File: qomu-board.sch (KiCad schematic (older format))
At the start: 37 parts, among them IC1 EOS-S3, SW2 Captouch Pads, U1 LDO-X2SON-1.2V, U10 RGB-LED, U2 LDO-X2SON-3.3V, U3 LDO-X2SON-2.5V, U4 GD25Q16CEIGR, U5 MC3635, U9 USB-B

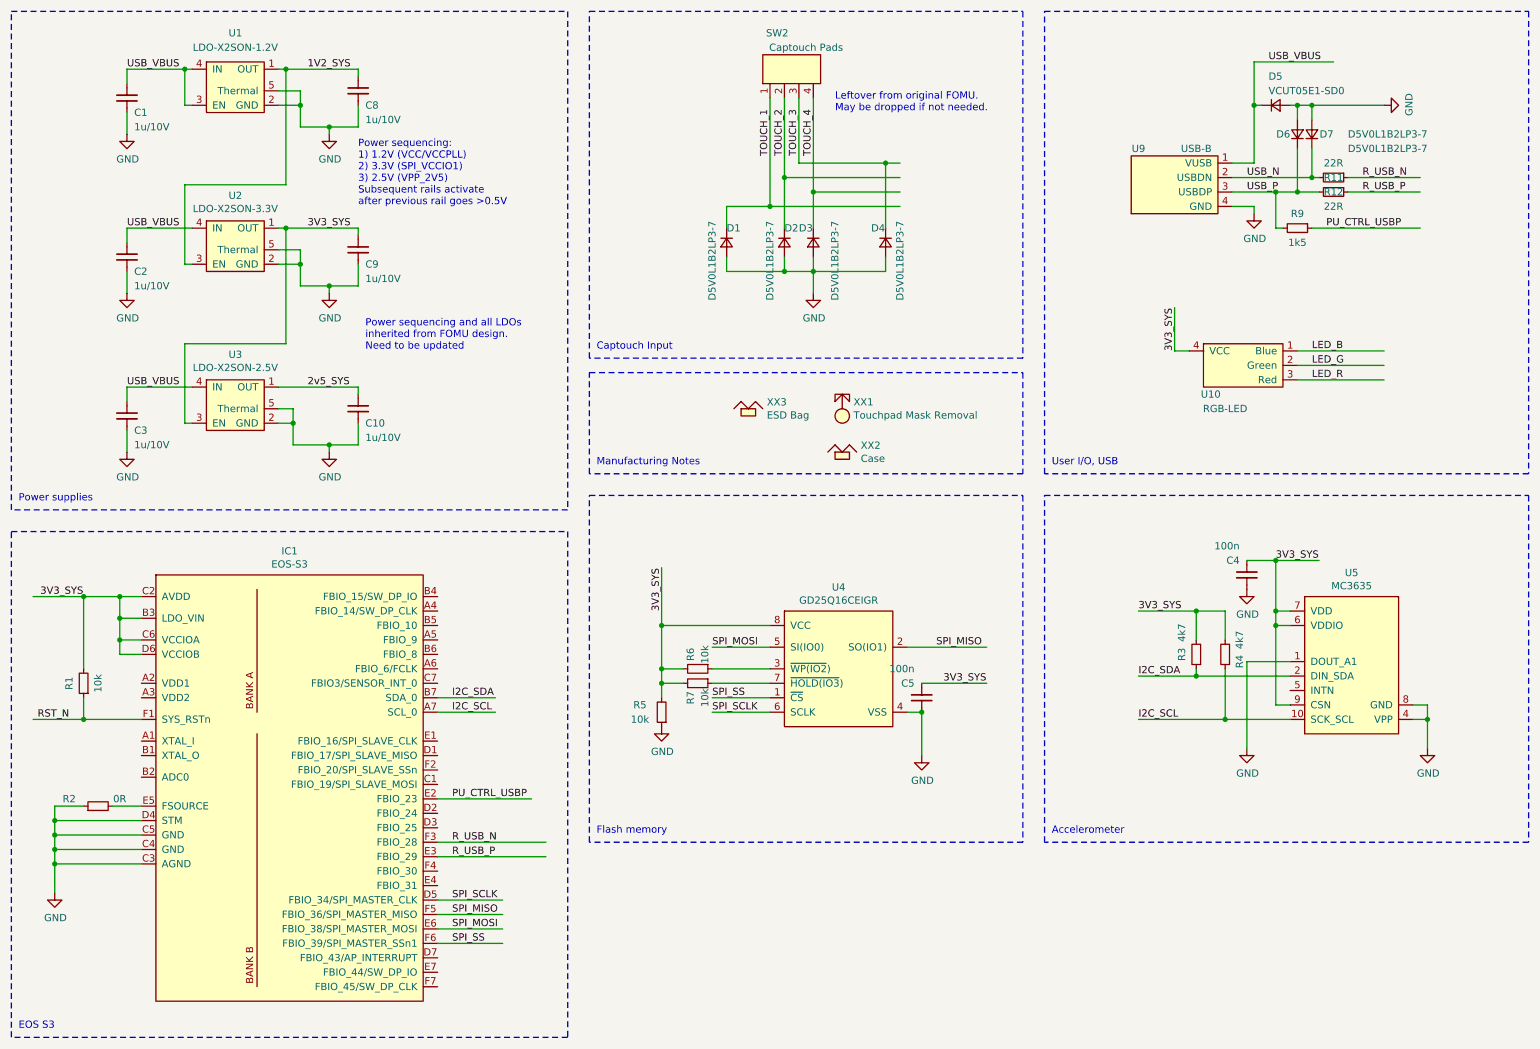
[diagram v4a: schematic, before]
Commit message: Added single LDO as power supply, cleanup
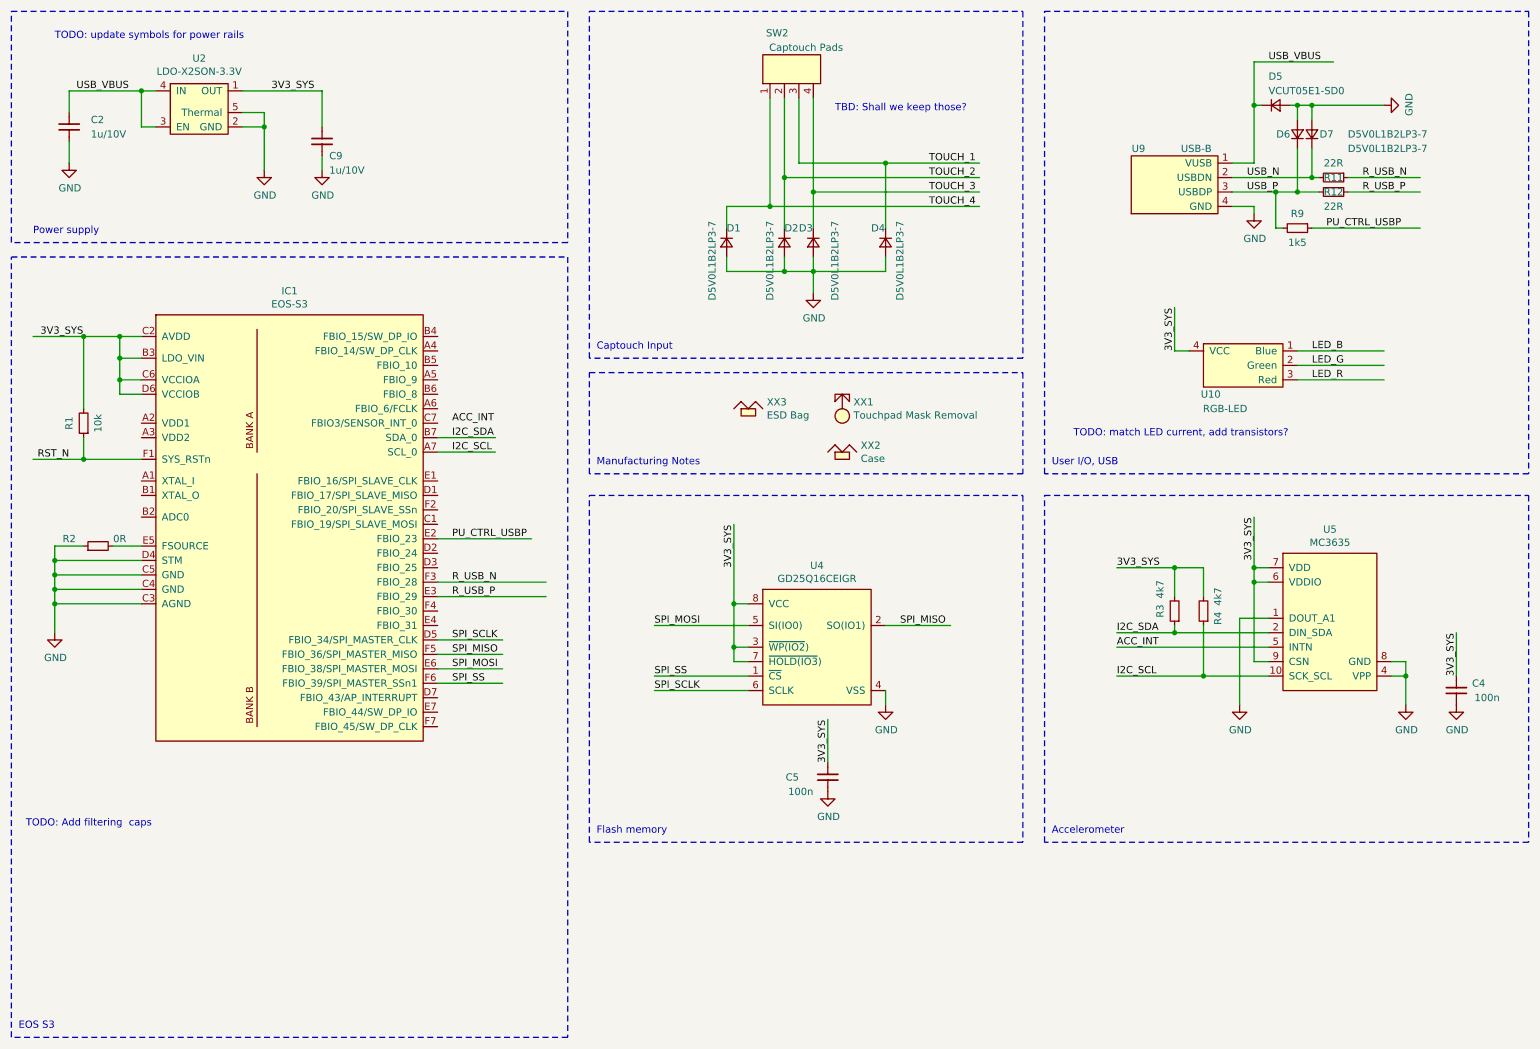
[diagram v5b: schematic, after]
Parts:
- removed C1, C10, C3, C8: 1u/10V, qomu-board:C_0201_0603Metric, symbol qomu-board:C_Small-Device
- removed R5, R6, R7: 10k, qomu-board:R_0201_0603Metric, symbol qomu-board:R_Small-Device
- removed U1: LDO-X2SON-1.2V, qomu-board:Texas_X2SON-4_1x1mm_P0.65mm, symbol qomu-board:LDO-X2SON
- removed U3: LDO-X2SON-2.5V, qomu-board:Texas_X2SON-4_1x1mm_P0.65mm, symbol qomu-board:LDO-X2SON
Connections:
- net labels added: ACC_INT
- net labels removed: 1V2_SYS, 2v5_SYS
- wire segments 176 -> 133
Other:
- note added: "Power supply"
- note added: "TBD: Shall we keep those?"
- note added: "TODO: Add filtering caps"
- note added: "TODO: match LED current, add transistors?"
- note added: "TODO: update symbols for power rails"
- note removed: "Leftover from original FOMU. \nMay be dropped if not needed."
- note removed: "Power sequencing and all LDOs\ninherited from FOMU design.\nNeed to be updated\n"
- note removed: "Power sequencing:\n1) 1.2V (VCC/VCCPLL)\n2) 3.3V (SPI_VCCIO1)\n3) 2.5V (VPP_2V5)\nSubsequent rails activate\nafter previous rail goes >0.5V"
- note removed: "Power supplies"
- moved on the sheet: C2, C4, C5, C9, IC1, R1, R2, R3, R4, U2, U4, U5

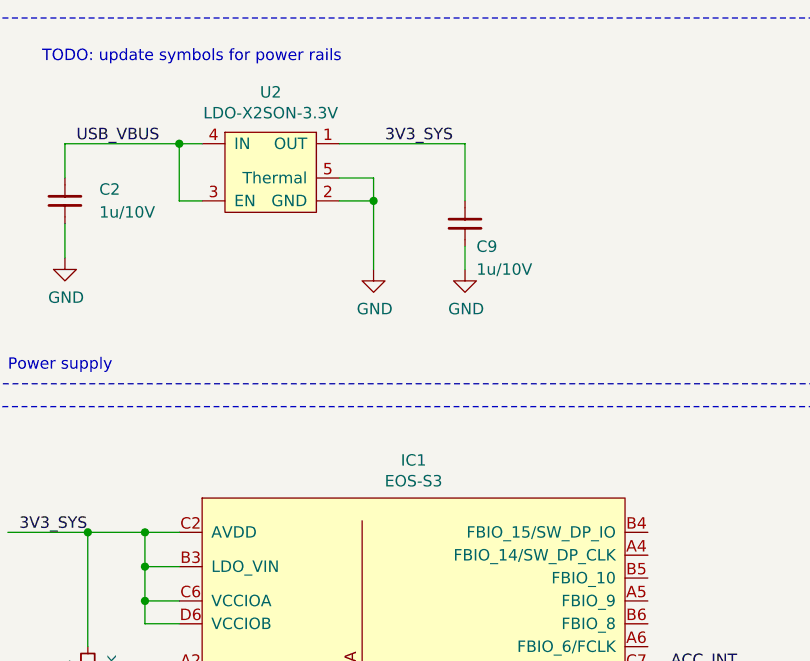
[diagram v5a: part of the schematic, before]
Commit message: Updated MPN for LDO
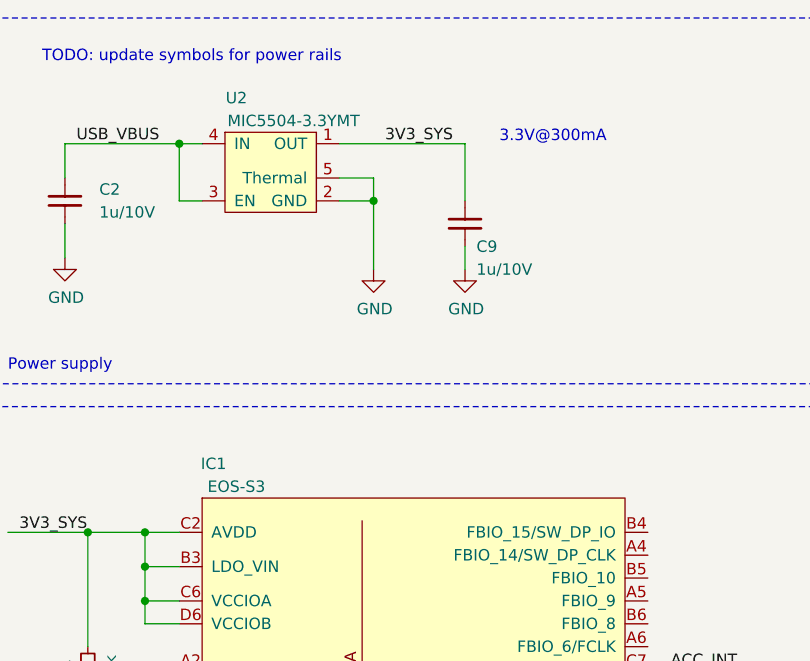
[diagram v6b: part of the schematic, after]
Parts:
- U2: value LDO-X2SON-3.3V -> MIC5504-3.3YMT; AManufacturer Microchip -> (none); APN 576-4305-1-ND -> (none); DPN 296-39066-2-ND -> (none); MPN LP5907SNX-3.3/NOPB -> MIC5504-3.3YMT; Manufacturer TI -> Microchip
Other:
- note added: "3.3V@300mA"
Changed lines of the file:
@@
 U 1 1 5DCB0652
 P 1600 2700
-F 0 "IC1" H 2525 2865 50  0000 C CNN
-F 1 "EOS-S3" H 2525 2774 50  0000 C CNN
+F 0 "IC1" H 1650 2850 50  0000 C CNN
+F 1 "EOS-S3" H 1750 2750 50  0000 C CNN
 F 2 "qomu-board:42-WLCSP" H 3250 -400 50  0001 C CNN
 F 3 "https://www.quicklogic.com/wp-content/uploads/2020/06/QL-EOS-S3-Ultra-Low-Power-multicore-MCU-Datasheet.pdf" H 3350 -300 50  0001 C CNN
@@
 U 1 1 5BF61C95
 P 1900 1450
-F 0 "U2" H 1900 1975 50  0000 C CNN
-F 1 "LDO-X2SON-3.3V" H 1900 1884 50  0000 C CNN
+F 0 "U2" H 1750 1950 50  0000 C CNN
+F 1 "MIC5504-3.3YMT" H 2000 1850 50  0000 C CNN
 F 2 "qomu-board:Texas_X2SON-4_1x1mm_P0.65mm" H 1900 1450 50  0001 C CNN
-F 3 "http://www.ti.com/lit/ds/symlink/lp5907.pdf" H 1900 1450 50  0001 C CNN
+F 3 "" H 1900 1450 50  0001 C CNN
 F 4 "MIC5504-3.3YMT" H 250 150 50  0001 C CNN "AMPN"
-F 5 "Microchip" H 250 150 50  0001 C CNN "AManufacturer"
-F 6 "576-4305-1-ND" H 250 150 50  0001 C CNN "APN"
-F 7 "LP5907SNX-3.3/NOPB" H 250 150 50  0001 C CNN "MPN"
-F 8 "TI" H 250 150 50  0001 C CNN "Manufacturer"
-F 9 "296-39066-2-ND " H 1900 1450 50  0001 C CNN "DPN"
+F 5 "" H 250 2750 50  0001 C CNN "AManufacturer"
+F 6 "" H 250 150 50  0001 C CNN "APN"
+F 7 "MIC5504-3.3YMT" H 250 150 50  0001 C CNN "MPN"
+F 8 "Microchip" H 250 150 50  0001 C CNN "Manufacturer"
+F 9 "" H 1900 1450 50  0001 C CNN "DPN"
 	1    1900 1450
 	1    0    0    -1
@@
 Text Notes 7950 3550 0    50   ~ 0
 TODO: match LED current, add transistors?
+Text Notes 2900 1150 0    50   ~ 0
+3.3V@300mA
 $EndSCHEMATC

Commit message: Minor changes
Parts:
- removed R2: 0R, qomu-board:R_0201_0603Metric, symbol qomu-board:R_Small-Device
- U10: value RGB-LED -> UHD1110-FKA
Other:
- note added: "5mA/channel"
- note removed: "TODO: match LED current, add transistors?"
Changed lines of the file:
@@
 P 9100 3200
 F 0 "U10" H 8900 3150 50  0000 C CNN
-F 1 "RGB-LED" H 9000 3050 50  0000 C CNN
+F 1 "UHD1110-FKA" H 9100 3050 50  0000 C CNN
 F 2 "qomu-board:LED-RGB-5DS-UHD1110-FKA" H 9100 3200 50  0001 C CNN
 F 3 "https://www.cree.com/led-components/media/documents/ds-UHD1110-FKA.pdf" H 9100 3200 50  0001 C CNN
@@
 	0    1    1    0
 $EndComp
-$Comp
-L qomu-board:R_Small-Device R2
-U 1 1 5DC79CE9
-P 1200 4300
-F 0 "R2" V 1250 4500 50  0000 C CNN
-F 1 "0R" V 1250 4150 50  0000 C CNN
-F 2 "qomu-board:R_0201_0603Metric" H 1200 4300 50  0001 C CNN
-F 3 "" H 1200 4300 50  0001 C CNN
-F 4 "ANY" H -7550 2600 50  0001 C CNN "MPN"
-	1    1200 4300
-	0    -1   -1   0
-$EndComp
-Wire Wire Line
-	1500 4300 1300 4300
-Wire Wire Line
-	1100 4300 900  4300
-Wire Wire Line
-	900  4300 900  4400
+Wire Wire Line
+	1300 4300 1300 4400
 $Comp
 L power:GND #PWR0101
 U 1 1 5DC830C3
-P 900 4900
-F 0 "#PWR0101" H 900 4650 50  0001 C CNN
-F 1 "GND" H 905 4727 50  0000 C CNN
-F 2 "" H 900 4900 50  0001 C CNN
-F 3 "" H 900 4900 50  0001 C CNN
-	1    900  4900
+P 1300 4900
+F 0 "#PWR0101" H 1300 4650 50  0001 C CNN
+F 1 "GND" H 1305 4727 50  0000 C CNN
+F 2 "" H 1300 4900 50  0001 C CNN
+F 3 "" H 1300 4900 50  0001 C CNN
+	1    1300 4900
 	1    0    0    -1
 $EndComp
@@
 USB_VBUS
 Wire Wire Line
-	1500 4400 900  4400
-Connection ~ 900  4400
-Wire Wire Line
-	900  4400 900  4500
-Wire Wire Line
-	1500 4500 900  4500
-Connection ~ 900  4500
-Wire Wire Line
-	900  4500 900  4600
-Wire Wire Line
-	1500 4600 900  4600
-Connection ~ 900  4600
-Wire Wire Line
-	900  4600 900  4700
-Wire Wire Line
-	1500 4700 900  4700
-Connection ~ 900  4700
-Wire Wire Line
-	900  4700 900  4900
+	1500 4400 1300 4400
+Connection ~ 1300 4400
+Wire Wire Line
+	1300 4400 1300 4500
+Wire Wire Line
+	1500 4500 1300 4500
+Connection ~ 1300 4500
+Wire Wire Line
+	1300 4500 1300 4600
+Wire Wire Line
+	1500 4600 1300 4600
+Connection ~ 1300 4600
+Wire Wire Line
+	1300 4600 1300 4700
+Wire Wire Line
+	1500 4700 1300 4700
+Connection ~ 1300 4700
+Wire Wire Line
+	1300 4700 1300 4900
 $Comp
 L qomu-board:C_Small-Device C2
@@
 Text Label 9200 4400 1    50   ~ 0
 3V3_SYS
-Text Notes 7950 3550 0    50   ~ 0
-TODO: match LED current, add transistors?
 Text Notes 2900 1150 0    50   ~ 0
 3.3V@300mA
+Text Notes 9550 2800 0    50   ~ 0
+5mA/channel
+Wire Wire Line
+	1300 4300 1500 4300
+Wire Wire Line
+	3550 3450 3950 3450
 $EndSCHEMATC

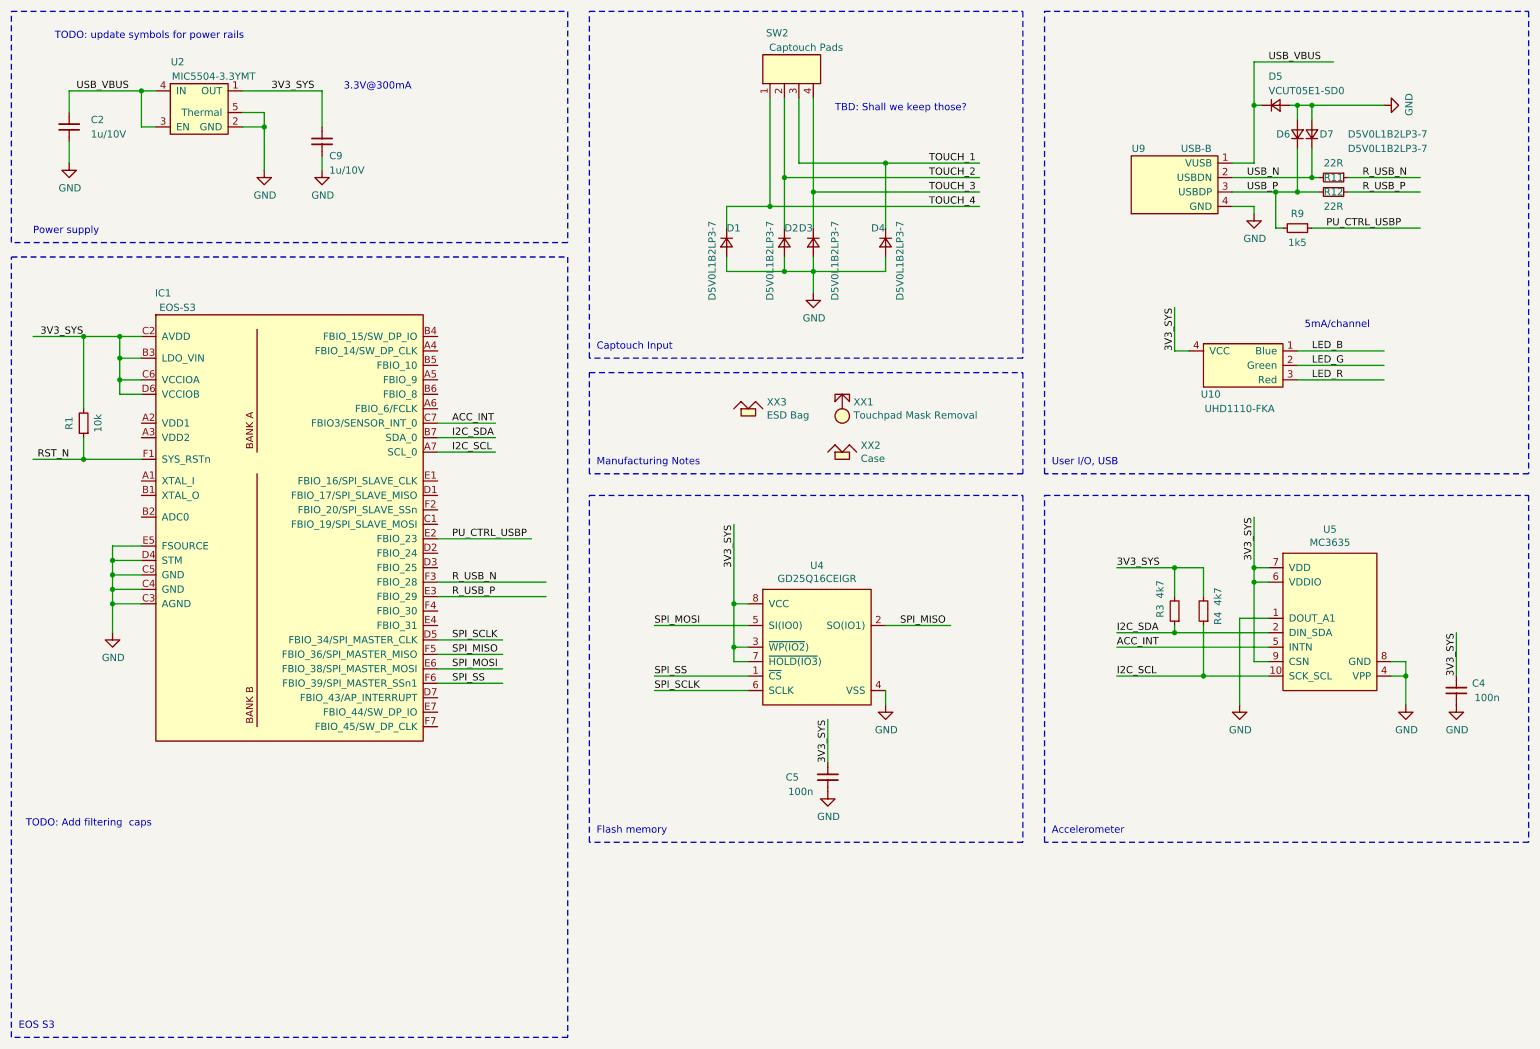
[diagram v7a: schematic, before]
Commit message: Added notes regarding power consumption
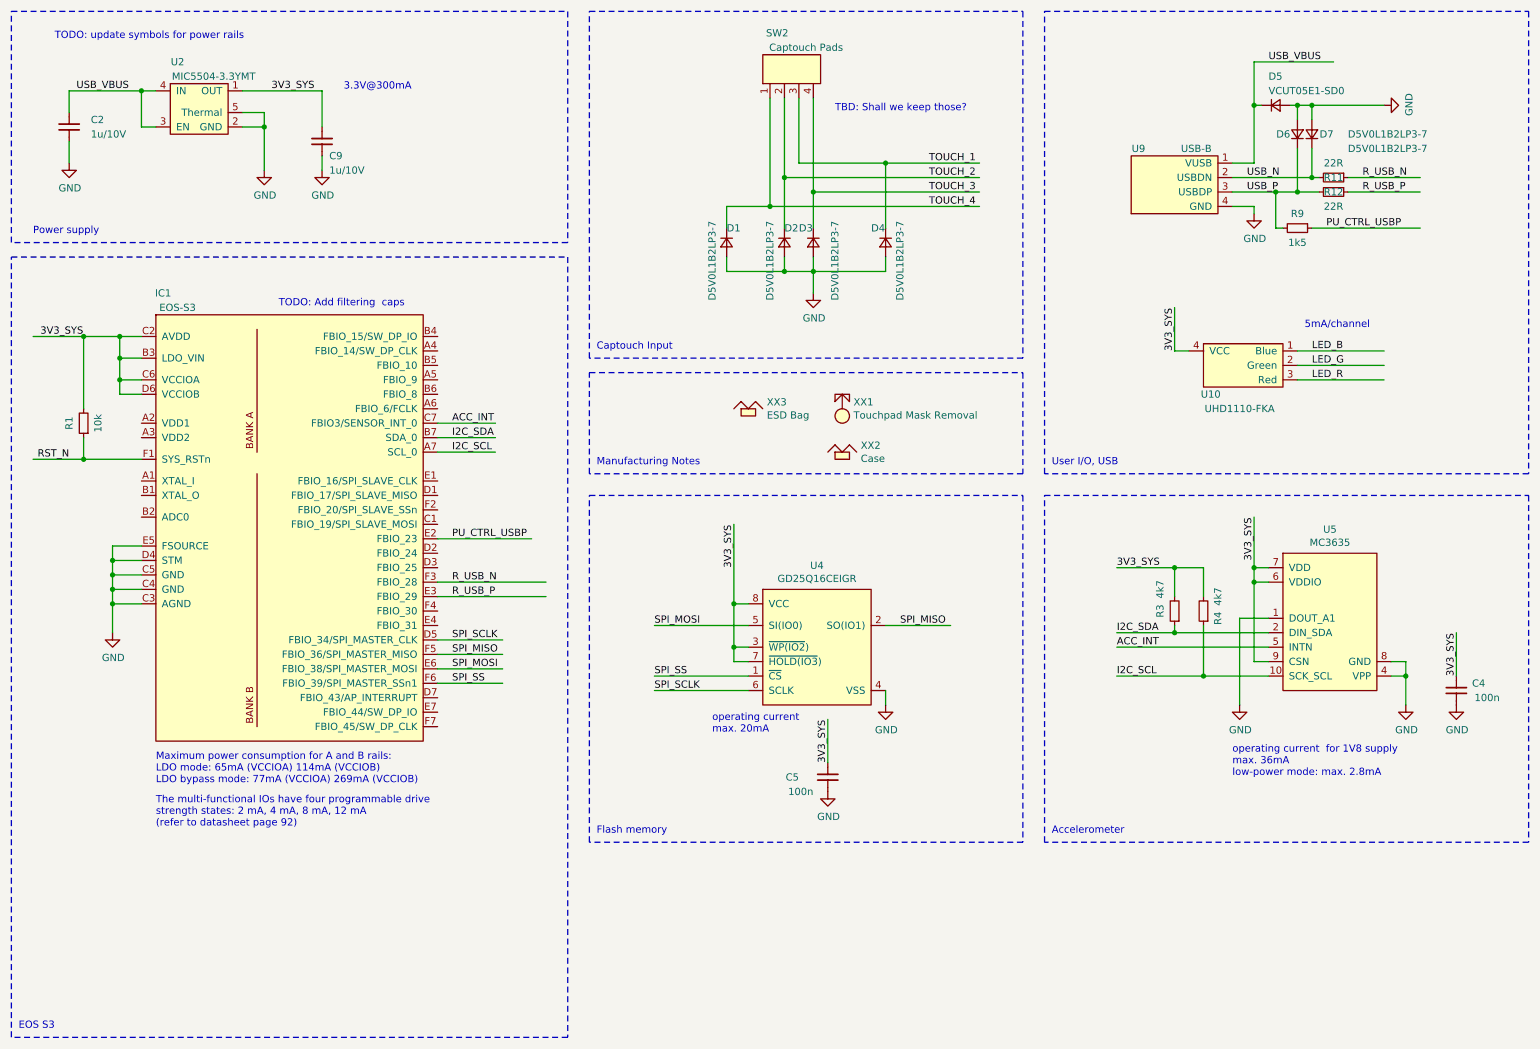
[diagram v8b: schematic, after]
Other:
- note added: "Maximum power consumption for A and B rails:\nLDO mode: 65mA (VCCIOA) 114mA (VCCIOB)\nLDO bypass mode: 77mA (VCCIOA) 269mA (VCCIOB)"
- note added: "The multi-functional IOs have four programmable drive \nstrength states: 2 mA, 4 mA, 8 mA, 12 mA \n(refer to datasheet page 92)"
- note added: "operating current for 1V8 supply\nmax. 36mA\nlow-power mode: max. 2.8mA\n"
- note added: "operating current\nmax. 20mA"
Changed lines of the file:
@@
 Wire Wire Line
 	5600 4150 5600 4700
-Text Notes 700  6250 0    50   ~ 0
+Text Notes 2450 2650 0    50   ~ 0
 TODO: Add filtering  caps
 Text Notes 900  800  0    50   ~ 0
@@
 Wire Wire Line
 	3550 3450 3950 3450
+Text Notes 5450 5600 0    50   ~ 0
+operating current\nmax. 20mA
+Text Notes 1600 5950 0    50   ~ 0
+Maximum power consumption for A and B rails:\nLDO mode: 65mA (VCCIOA) 114mA (VCCIOB)\nLDO bypass mode: 77mA (VCCIOA) 269mA (VCCIOB)
+Text Notes 1600 6250 0    50   ~ 0
+The multi-functional IOs have four programmable drive \nstrength states: 2 mA, 4 mA, 8 mA, 12 mA \n(refer to datasheet page 92)
+Text Notes 9050 5900 0    50   ~ 0
+operating current  for 1V8 supply\nmax. 36mA\nlow-power mode: max. 2.8mA\n
 $EndSCHEMATC
